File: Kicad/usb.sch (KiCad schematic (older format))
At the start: 25 parts, among them J501 USB Ports External, J502 USB Ports Internal, U501 AP2501, U502 MIC2005A-2YM5, U503 MIC2005A-2YM5, U504 XR22404CG28, U505 MIC2005A-2YM5, U506 MIC2005A-2YM5, Y501 12M

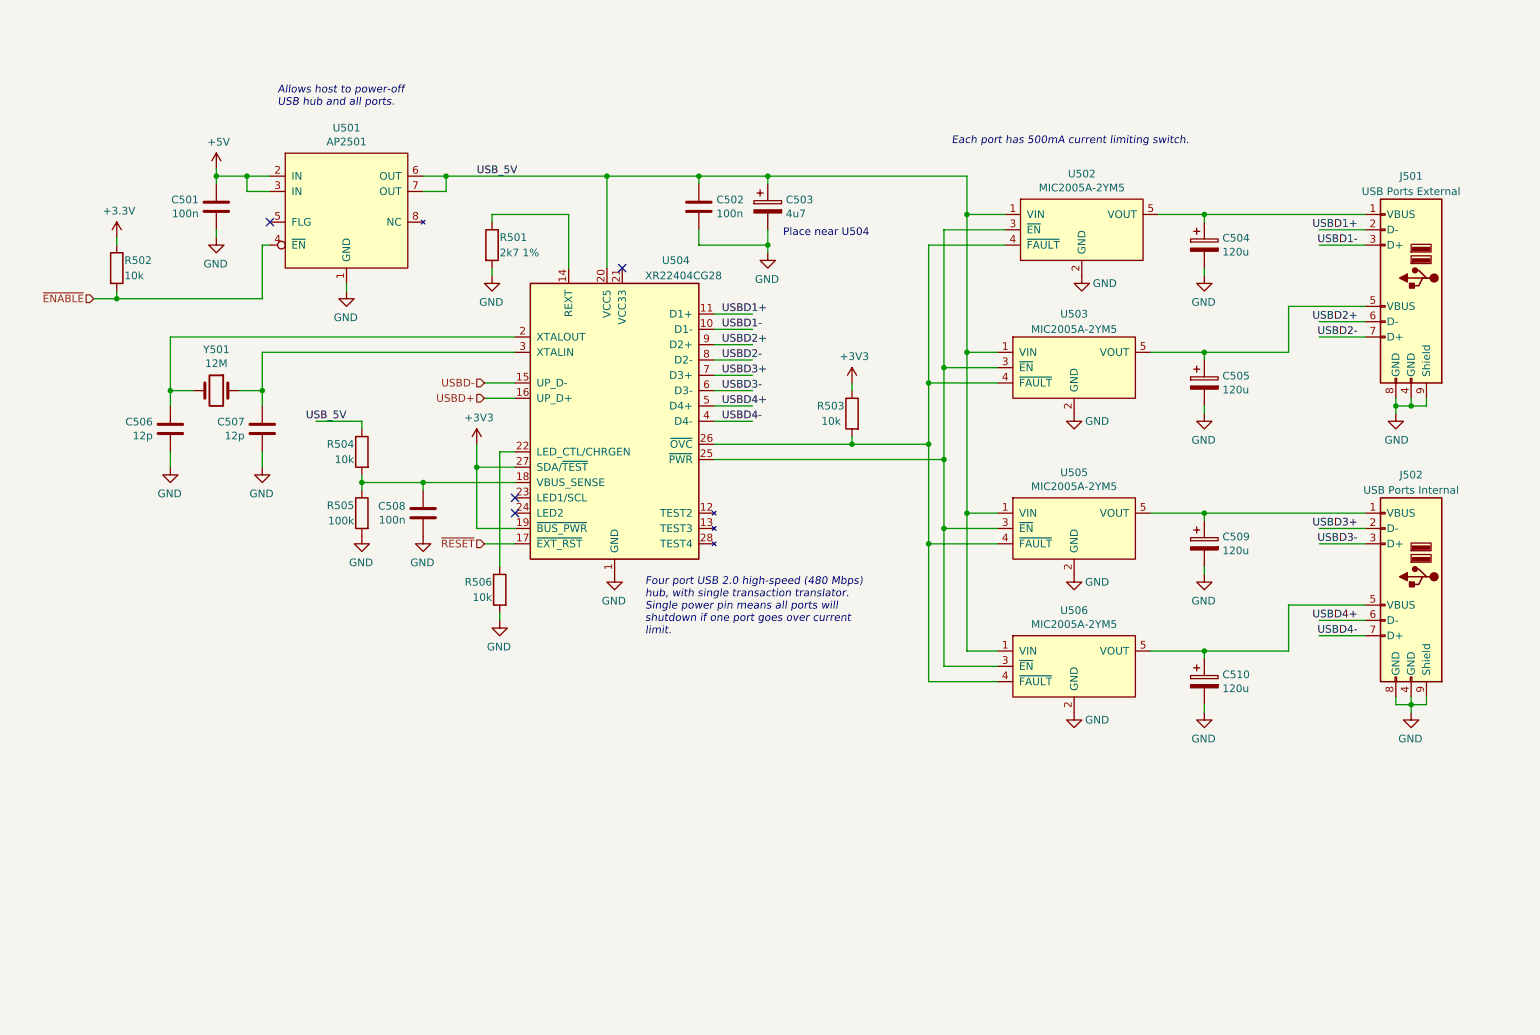
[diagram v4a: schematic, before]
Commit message: Make CPU card bigger.
Just big enough to take a TQFP-176 now.
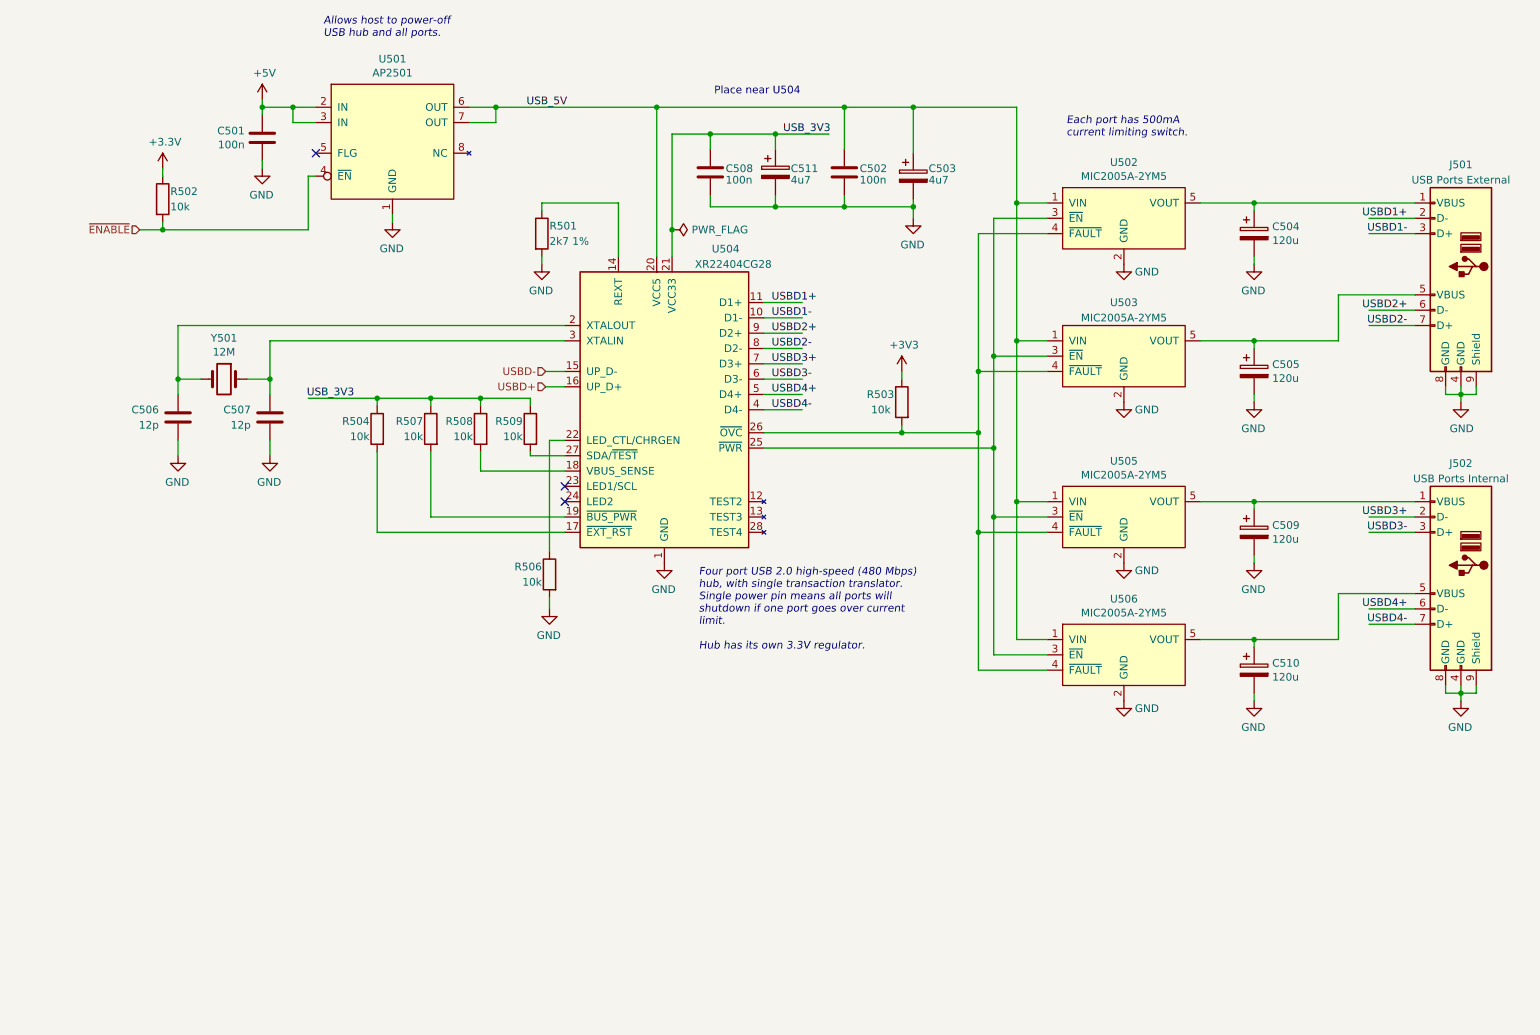
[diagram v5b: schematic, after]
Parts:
- removed R505: 100k, Resistor_SMD:R_0805_2012Metric_Pad1.15x1.40mm_HandSolder, symbol Device:R
- added C511: 4u7, Capacitor_THT:CP_Radial_D6.3mm_P2.50mm, symbol Device:CP
- added R507, R508, R509: 10k, Resistor_SMD:R_0805_2012Metric_Pad1.15x1.40mm_HandSolder, symbol Device:R
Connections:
- net labels added: USB_3V3
- net labels removed: ~RESET
- wire segments 136 -> 151
- no-connect marks 4 -> 3
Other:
- note added: "Each port has 500mA\ncurrent limiting switch."
- note added: "Four port USB 2.0 high-speed (480 Mbps)\nhub, with single transaction translator.\nSingle power pin means all ports will\nshutdown if one port goes over current\nlimit.\n\nHub has its own 3.3V regulator."
- note removed: "Each port has 500mA current limiting switch."
- note removed: "Four port USB 2.0 high-speed (480 Mbps)\nhub, with single transaction translator.\nSingle power pin means all ports will\nshutdown if one port goes over current\nlimit."
- moved on the sheet: C501, C502, C503, C504, C505, C506, C507, C509, C510, J501, J502, R501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

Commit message: Bring in R2R DAC from Neotron-9X schematic.
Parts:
- renumbered C501 to C1001, C508 to C1002, C511 to C1003, C502 to C1004, C503 to C1005, C504 to C1006, C505 to C1007, C506 to C1008, C507 to C1009, C509 to C1010, C510 to C1011, J501 to J1001, J502 to J1002, R502 to R1001, R501 to R1002, R503 to R1003, R504 to R1004, R507 to R1005, R508 to R1006, R509 to R1007, R506 to R1008, U501 to U1001, U502 to U1002, U503 to U1003, U504 to U1004, U505 to U1005, U506 to U1006, Y501 to Y1001

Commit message: Added some part numbers.
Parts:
- C1003, C1005: Digikey (none) -> 493-12612-1-ND; MPN (none) -> UVK2A4R7MDD1TD; Manufacturer (none) -> Nichicon
- C1006, C1007, C1010, C1011: footprint Capacitor_THT:CP_Radial_D6.3mm_P2.50mm -> Capacitor_THT:CP_Radial_D8.0mm_P3.50mm; Digikey (none) -> 493-17035-ND; MPN (none) -> UPJ1H121MPD; Manufacturer (none) -> Nichicon
- C1008, C1009: Digikey (none) -> 1276-2580-1-ND; MPN (none) -> CL21C120JB61PNC; Manufacturer (none) -> Samsung
- R1001, R1003, R1004, R1005, R1006, R1007, R1008: Digikey (none) -> RMCF0805FT10K0-ND; MPN (none) -> RMCF0805FT10K0
- R1002: Digikey (none) -> RMCF0805FT2K70CT-ND; MPN (none) -> RMCF0805FT2K70; Manufacturer (none) -> Stackpole
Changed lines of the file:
@@
 F 3 "~" H 6275 3425 50  0001 C CNN
 F 4 "0" H 6275 3425 50  0001 C CNN "DNP"
+F 5 "RMCF0805FT10K0-ND" H 6275 3425 50  0001 C CNN "Digikey"
+F 6 "RMCF0805FT10K0" H 6275 3425 50  0001 C CNN "MPN"
 	1    6275 3425
 	-1   0    0    -1
@@
 F 3 "~" H 1550 3525 50  0001 C CNN
 F 4 "0" H 1550 3525 50  0001 C CNN "DNP"
+F 5 "1276-2580-1-ND" H 1550 3525 50  0001 C CNN "Digikey"
+F 6 "CL21C120JB61PNC" H 1550 3525 50  0001 C CNN "MPN"
+F 7 "Samsung" H 1550 3525 50  0001 C CNN "Manufacturer"
 	1    1550 3525
 	-1   0    0    -1
@@
 F 3 "~" H 2150 3525 50  0001 C CNN
 F 4 "0" H 2150 3525 50  0001 C CNN "DNP"
+F 5 "1276-2580-1-ND" H 2150 3525 50  0001 C CNN "Digikey"
+F 6 "CL21C120JB61PNC" H 2150 3525 50  0001 C CNN "MPN"
+F 7 "Samsung" H 2150 3525 50  0001 C CNN "Manufacturer"
 	1    2150 3525
 	-1   0    0    -1
@@
 F 3 "~" H 6350 1950 50  0001 C CNN
 F 4 "0" H 6350 1950 50  0001 C CNN "DNP"
+F 5 "493-12612-1-ND" H 6350 1950 50  0001 C CNN "Digikey"
+F 6 "UVK2A4R7MDD1TD" H 6350 1950 50  0001 C CNN "MPN"
+F 7 "Nichicon" H 6350 1950 50  0001 C CNN "Manufacturer"
 	1    6350 1950
 	1    0    0    -1
@@
 F 3 "~" H 3925 2325 50  0001 C CNN
 F 4 "0" H 3925 2325 50  0001 C CNN "DNP"
+F 5 "RMCF0805FT2K70CT-ND" H 3925 2325 50  0001 C CNN "Digikey"
+F 6 "RMCF0805FT2K70" H 3925 2325 50  0001 C CNN "MPN"
+F 7 "Stackpole" H 3925 2325 50  0001 C CNN "Manufacturer"
 	1    3925 2325
 	1    0    0    -1
@@
 F 0 "C1006" H 8693 2371 50  0000 L CNN
 F 1 "120u" H 8693 2280 50  0000 L CNN
-F 2 "Capacitor_THT:CP_Radial_D6.3mm_P2.50mm" H 8613 2175 50  0001 C CNN
+F 2 "Capacitor_THT:CP_Radial_D8.0mm_P3.50mm" H 8613 2175 50  0001 C CNN
 F 3 "~" H 8575 2325 50  0001 C CNN
 F 4 "0" H 8575 2325 50  0001 C CNN "DNP"
+F 5 "493-17035-ND" H 8575 2325 50  0001 C CNN "Digikey"
+F 6 "UPJ1H121MPD" H 8575 2325 50  0001 C CNN "MPN"
+F 7 "Nichicon" H 8575 2325 50  0001 C CNN "Manufacturer"
 	1    8575 2325
 	1    0    0    -1
@@
 F 0 "C1007" H 8693 3271 50  0000 L CNN
 F 1 "120u" H 8693 3180 50  0000 L CNN
-F 2 "Capacitor_THT:CP_Radial_D6.3mm_P2.50mm" H 8613 3075 50  0001 C CNN
+F 2 "Capacitor_THT:CP_Radial_D8.0mm_P3.50mm" H 8613 3075 50  0001 C CNN
 F 3 "~" H 8575 3225 50  0001 C CNN
 F 4 "0" H 8575 3225 50  0001 C CNN "DNP"
+F 5 "493-17035-ND" H 8575 3225 50  0001 C CNN "Digikey"
+F 6 "UPJ1H121MPD" H 8575 3225 50  0001 C CNN "MPN"
+F 7 "Nichicon" H 8575 3225 50  0001 C CNN "Manufacturer"
 	1    8575 3225
 	1    0    0    -1
@@
 F 0 "C1010" H 8693 4321 50  0000 L CNN
 F 1 "120u" H 8693 4230 50  0000 L CNN
-F 2 "Capacitor_THT:CP_Radial_D6.3mm_P2.50mm" H 8613 4125 50  0001 C CNN
+F 2 "Capacitor_THT:CP_Radial_D8.0mm_P3.50mm" H 8613 4125 50  0001 C CNN
 F 3 "~" H 8575 4275 50  0001 C CNN
 F 4 "0" H 8575 4275 50  0001 C CNN "DNP"
+F 5 "493-17035-ND" H 8575 4275 50  0001 C CNN "Digikey"
+F 6 "UPJ1H121MPD" H 8575 4275 50  0001 C CNN "MPN"
+F 7 "Nichicon" H 8575 4275 50  0001 C CNN "Manufacturer"
 	1    8575 4275
 	1    0    0    -1
@@
 F 0 "C1011" H 8693 5221 50  0000 L CNN
 F 1 "120u" H 8693 5130 50  0000 L CNN
-F 2 "Capacitor_THT:CP_Radial_D6.3mm_P2.50mm" H 8613 5025 50  0001 C CNN
+F 2 "Capacitor_THT:CP_Radial_D8.0mm_P3.50mm" H 8613 5025 50  0001 C CNN
 F 3 "~" H 8575 5175 50  0001 C CNN
 F 4 "0" H 8575 5175 50  0001 C CNN "DNP"
+F 5 "493-17035-ND" H 8575 5175 50  0001 C CNN "Digikey"
+F 6 "UPJ1H121MPD" H 8575 5175 50  0001 C CNN "MPN"
+F 7 "Nichicon" H 8575 5175 50  0001 C CNN "Manufacturer"
 	1    8575 5175
 	1    0    0    -1
@@
 F 3 "~" H 2850 3600 50  0001 C CNN
 F 4 "0" H 2850 3600 50  0001 C CNN "DNP"
+F 5 "RMCF0805FT10K0-ND" H 2850 3600 50  0001 C CNN "Digikey"
+F 6 "RMCF0805FT10K0" H 2850 3600 50  0001 C CNN "MPN"
 	1    2850 3600
 	-1   0    0    -1
@@
 F 3 "~" H 10075 4925 50  0001 C CNN
 F 4 "0" H 9925 4875 50  0001 C CNN "DNP"
+F 5 "~" H 9925 4875 50  0001 C CNN "Digikey"
+F 6 "~" H 9925 4875 50  0001 C CNN "MPN"
+F 7 "~" H 9925 4875 50  0001 C CNN "Manufacturer"
 	1    9925 4875
 	-1   0    0    -1
@@
 F 3 "~" H 3975 4550 50  0001 C CNN
 F 4 "0" H 3975 4550 50  0001 C CNN "DNP"
+F 5 "RMCF0805FT10K0-ND" H 3975 4550 50  0001 C CNN "Digikey"
+F 6 "RMCF0805FT10K0" H 3975 4550 50  0001 C CNN "MPN"
 	1    3975 4550
 	-1   0    0    -1
@@
 F 3 "~" H 1450 2100 50  0001 C CNN
 F 4 "0" H 1450 2100 50  0001 C CNN "DNP"
+F 5 "RMCF0805FT10K0-ND" H 1450 2100 50  0001 C CNN "Digikey"
+F 6 "RMCF0805FT10K0" H 1450 2100 50  0001 C CNN "MPN"
 	1    1450 2100
 	1    0    0    -1
@@
 F 3 "~" H 5450 1925 50  0001 C CNN
 F 4 "0" H 5450 1925 50  0001 C CNN "DNP"
+F 5 "493-12612-1-ND" H 5450 1925 50  0001 C CNN "Digikey"
+F 6 "UVK2A4R7MDD1TD" H 5450 1925 50  0001 C CNN "MPN"
+F 7 "Nichicon" H 5450 1925 50  0001 C CNN "Manufacturer"
 	1    5450 1925
 	1    0    0    -1
@@
 F 3 "~" H 3850 3600 50  0001 C CNN
 F 4 "0" H 3850 3600 50  0001 C CNN "DNP"
+F 5 "RMCF0805FT10K0-ND" H 3850 3600 50  0001 C CNN "Digikey"
+F 6 "RMCF0805FT10K0" H 3850 3600 50  0001 C CNN "MPN"
 	1    3850 3600
 	-1   0    0    -1
@@
 F 3 "~" H 3525 3600 50  0001 C CNN
 F 4 "0" H 3525 3600 50  0001 C CNN "DNP"
+F 5 "RMCF0805FT10K0-ND" H 3525 3600 50  0001 C CNN "Digikey"
+F 6 "RMCF0805FT10K0" H 3525 3600 50  0001 C CNN "MPN"
 	1    3525 3600
 	-1   0    0    -1
@@
 F 3 "~" H 3200 3600 50  0001 C CNN
 F 4 "0" H 3200 3600 50  0001 C CNN "DNP"
+F 5 "RMCF0805FT10K0-ND" H 3200 3600 50  0001 C CNN "Digikey"
+F 6 "RMCF0805FT10K0" H 3200 3600 50  0001 C CNN "MPN"
 	1    3200 3600
 	-1   0    0    -1
